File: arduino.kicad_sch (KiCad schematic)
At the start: 1 part

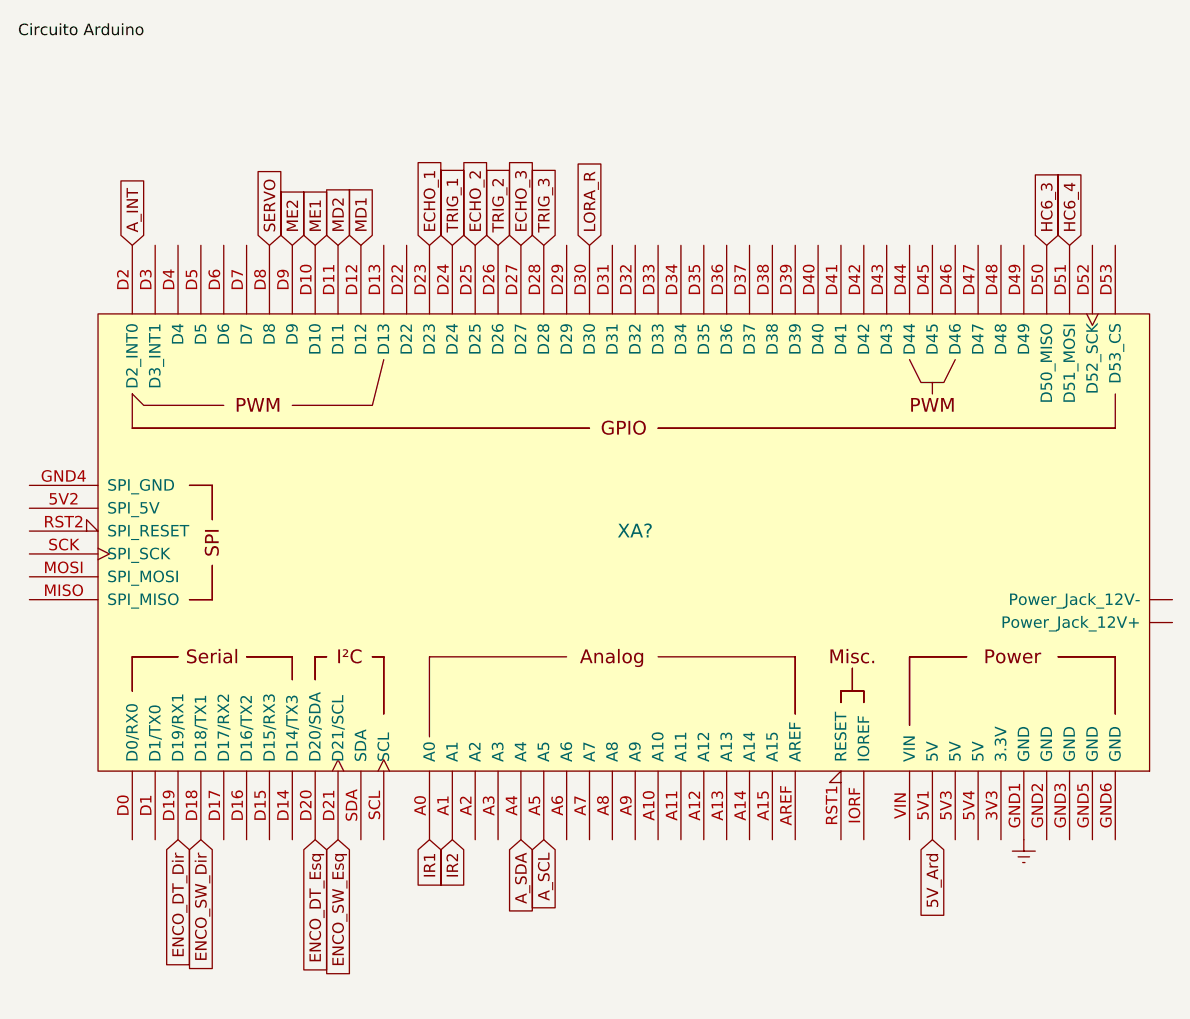
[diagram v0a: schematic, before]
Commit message: fix: modificado saídas do arduino
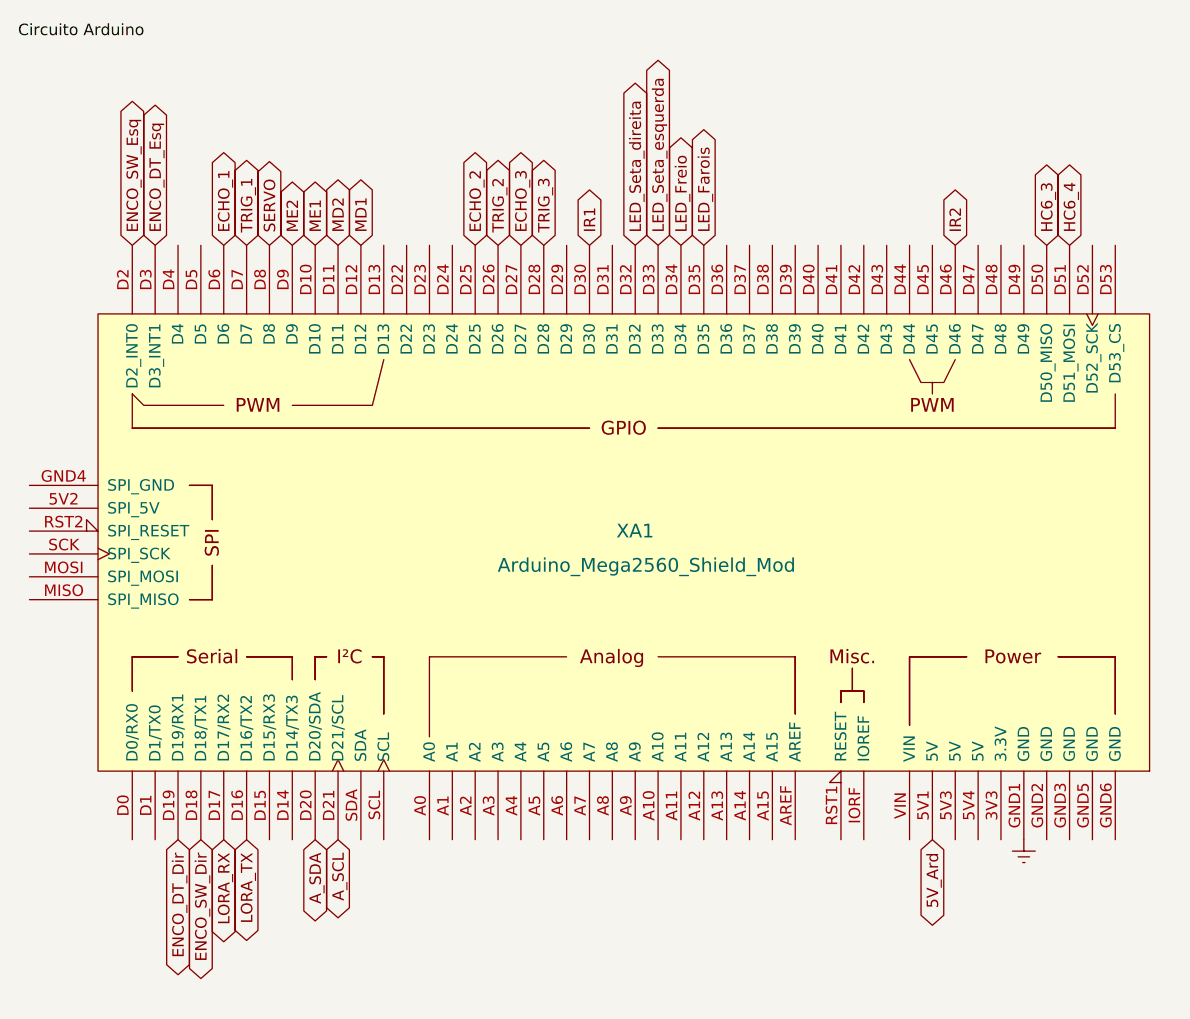
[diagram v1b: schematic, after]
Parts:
- XA1: renamed from XA?; value (none) -> Arduino_Mega2560_Shield_Mod; footprint (none) -> PCM_arduino-library:Arduino_Mega2560_R3_Shield; symbol PCM_arduino-library:Arduino_Mega2560_Shield_Mod -> PCM_arduino-library:Arduino_Mega2560_R3_Shield
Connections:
- net A_INT is gone; now on net ENCO_SW_Esq: XA1.D2 (D2_INT0)
- net LORA_R is gone; now on net IR1: XA1.D30
- net A_SCL: now also XA1.D21 (D21/SCL); no longer XA1.A5
- net A_SDA: now also XA1.D20 (D20/SDA); no longer XA1.A4
- net ECHO_1: now also XA1.D6; no longer XA1.D23
- net ENCO_DT_Esq: now also XA1.D3 (D3_INT1); no longer XA1.D20 (D20/SDA)
- net ENCO_SW_Esq: no longer XA1.D21 (D21/SCL)
- net IR1: no longer XA1.A0
- net IR2: now also XA1.D46; no longer XA1.A1
- net TRIG_1: now also XA1.D7; no longer XA1.D24
- net LORA_TX: now reaches XA1.D16 (D16/TX2)
- net LORA_RX: now reaches XA1.D17 (D17/RX2)
- net LED_Seta_direita: now reaches XA1.D32
- net LED_Seta_esquerda: now reaches XA1.D33
- net LED_Freio: now reaches XA1.D34
- net LED_Farois: now reaches XA1.D35

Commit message: fix: esquematico atualizado
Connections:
- net U_PlaSol: now reaches XA1.A10
- net U_Mot: now reaches XA1.A8
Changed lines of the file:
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@@
     (effects (font (size 1.27 1.27)) (justify left bottom))
+  )
+  (global_label "U_Mot" (shape bidirectional) (at 93.98 116.84 270) (fields_autoplaced)
+    (effects (font (size 1.27 1.27)) (justify right))
+    (property "Intersheetrefs" "${INTERSHEET_REFS}" (at 93.98 126.5607 90)
+      (effects (font (size 1.27 1.27)) (justify right))
+    )
   )
   (global_label "TRIG_2" (shape bidirectional) (at 81.28 50.8 90) (fields_autoplaced)
@@
     )
   )
+  (global_label "U_PlaSol" (shape bidirectional) (at 99.06 116.84 270) (fields_autoplaced)
+    (effects (font (size 1.27 1.27)) (justify right))
+    (property "Intersheetrefs" "${INTERSHEET_REFS}" (at 99.06 129.3425 90)
+      (effects (font (size 1.27 1.27)) (justify right))
+    )
+  )
